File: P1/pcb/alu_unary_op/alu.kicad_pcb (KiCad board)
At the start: 4 copper layers, 100.3 x 100.3 mm, 21 parts, among them J1 650473-5, U13 74LS541, U23 74HC04, U24 74HC04, U25 74LS621, U26 74LS157, U27 74LS157, U28 74LS621, U29 74HC238, U30 74LS32

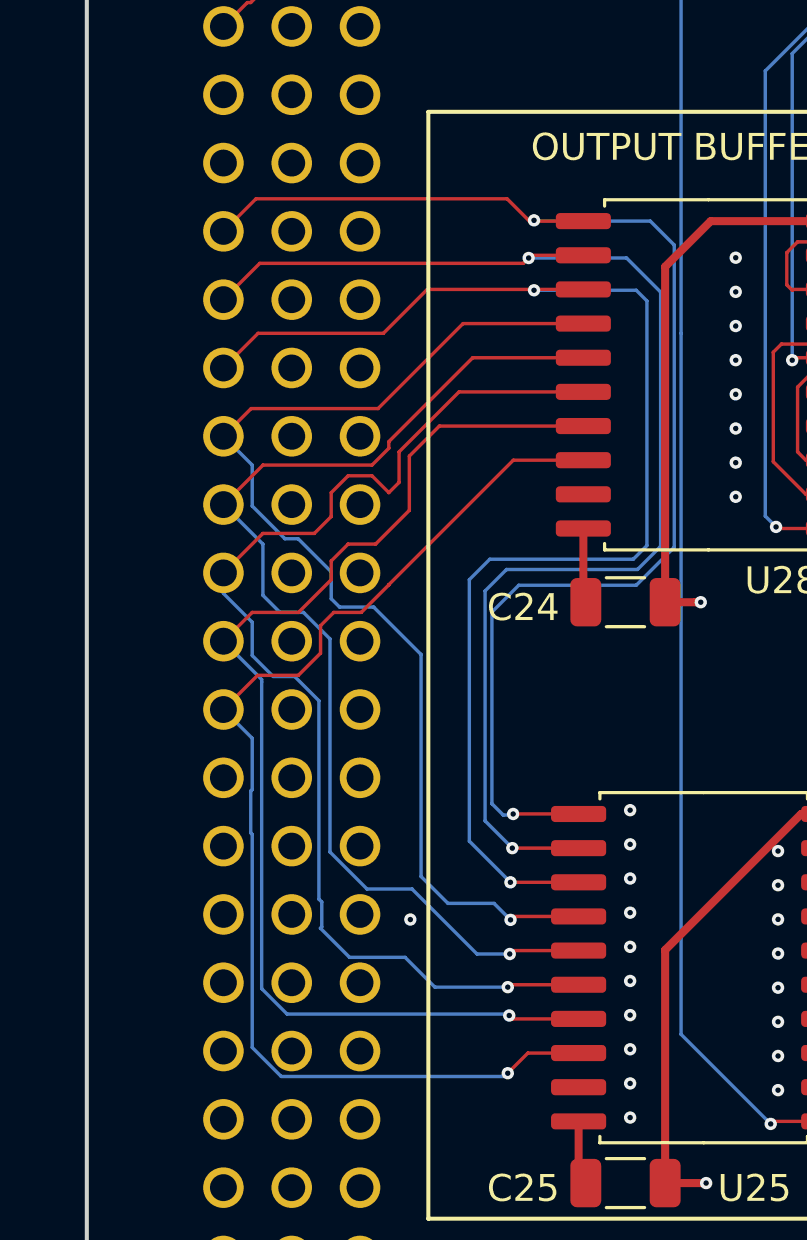
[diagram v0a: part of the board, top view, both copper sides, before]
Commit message: Removed unneeded backup files
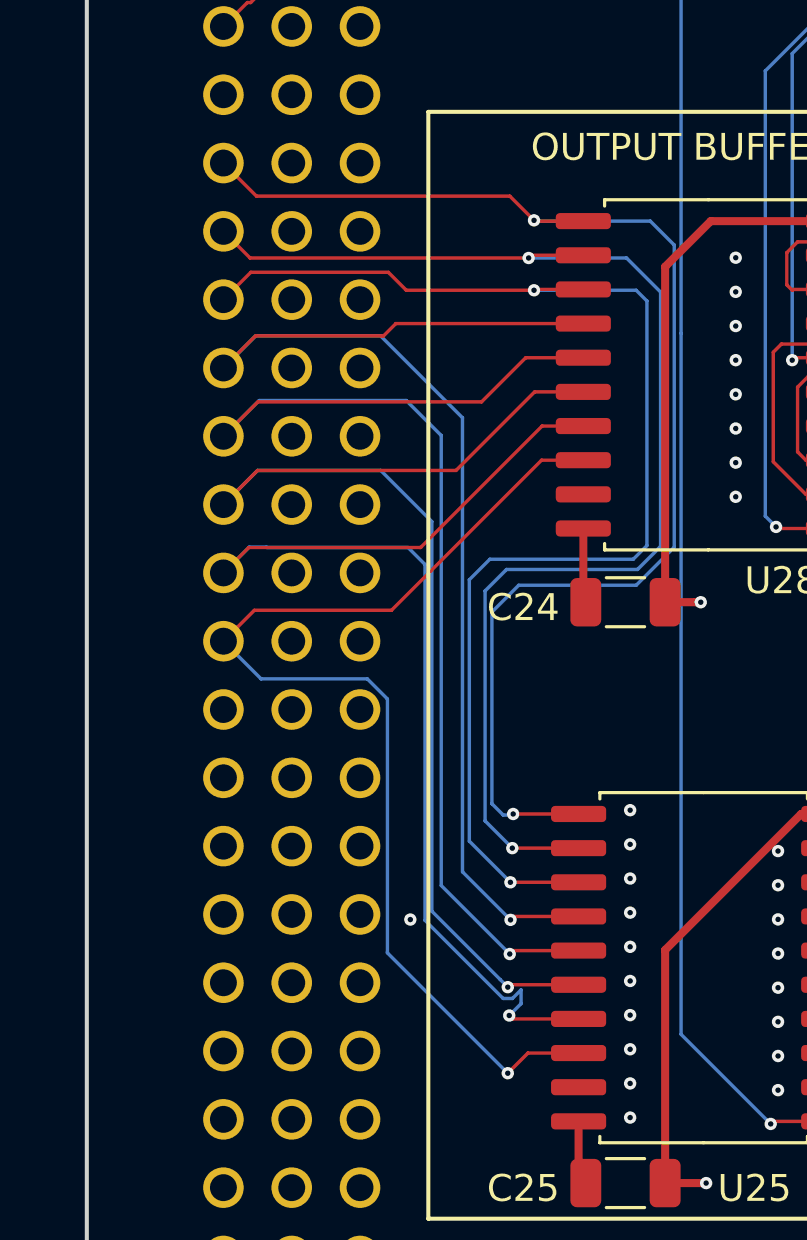
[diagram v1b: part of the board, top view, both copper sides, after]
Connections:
- J1 pad A18: /X_IN0 -> GND
- J1 pad A19: /X_IN1 -> /X_IN0
- J1 pad A20: /X_IN2 -> /X_IN1
- J1 pad A21: /X_IN3 -> /X_IN2
- J1 pad A22: /X_IN4 -> /X_IN3
- J1 pad A23: /X_IN5 -> /X_IN4
- J1 pad A24: /X_IN6 -> /X_IN5
- J1 pad A25: /X_IN7 -> /X_IN6
- J1 pad A26: unconnected-(J1-PadA26) -> /X_IN7
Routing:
- net GND: track 199.6 -> 205.7 mm
- net /X_IN3: track 41.7 -> 46.7 mm
- net /X_IN4: track 42.1 -> 46.7 mm
- net /X_IN0: track 44.1 -> 42.0 mm
- net /X_IN1: track 44.1 -> 45.8 mm
- net /X_IN2: track 43.9 -> 45.5 mm
- net /X_IN5: track 50.0 -> 49.4 mm
